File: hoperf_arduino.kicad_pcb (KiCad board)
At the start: 2 copper layers, 46 parts, among them J1 Conn_01x08_Male, J2 Conn_01x08_Male, Q1 DMN6140L, Q10 DMN6140L, Q11 DMN6140L, Q2 DMN6140L, Q3 DMN6140L, Q4 DMN6140L, Q5 DMN6140L, Q6 DMN6140L, Q7 DMN6140L, Q8 DMN6140L, Q9 DMN6140L, SW1 SW_SPST, U1 AZ1117-3.3, U2 RFM95W-915S2

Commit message: update sch and added routed pcb
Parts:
- removed J1, J2: Conn_01x08_Male, Connector_PinHeader_2.54mm:PinHeader_1x08_P2.54mm_Vertical
- added A1: Arduino_Nano_v3.x, Module:Arduino_Nano, F.Cu at (85.1, 120.7)
- added BT1: Battery_Cell, Connector_PinSocket_2.54mm:PinSocket_1x02_P2.54mm_Vertical, F.Cu at (156.2, 123.2)
- added FC1: FC-28, Connector_PinSocket_2.54mm:PinSocket_1x04_P2.54mm_Vertical, F.Cu at (62.2, 105.4)
- C1, C2, C3: footprint Capacitor_SMD:C_0603_1608Metric -> Capacitor_SMD:C_0603_1608Metric_Pad1.08x0.95mm_HandSolder
- D1: footprint LED_SMD:LED_0603_1608Metric -> LED_SMD:LED_0603_1608Metric_Pad1.05x0.95mm_HandSolder
- FB1, R1, R10, R11, R12, R13, R14, R15, R16, R17, R18, R19, R2, R20, R21, R22, R23, R24, R3, R4, R5, R6, R7, R8, R9: footprint Resistor_SMD:R_0603_1608Metric -> Resistor_SMD:R_0603_1608Metric_Pad0.98x0.95mm_HandSolder
- SW1: footprint Button_Switch_SMD:SW_SPST_SKQG_WithoutStem -> Button_Switch_SMD:SW_Push_1P1T_NO_CK_KSC7xxJ
- U1: footprint Package_TO_SOT_SMD:SOT-223-3_TabPin2 -> AZ1117CR-3.3:Diodes_Inc.-SOT89-03_2017-0-MFG
- moved R18 60.5 mm to (108.2, 111.4), turned to 270 degrees
- moved R19 58.4 mm to (110.2, 111.4), turned to 270 degrees
- moved R10 58.1 mm to (99.3, 95.2), turned to 270 degrees
- moved R11 56.6 mm to (101.3, 95.2), turned to 270 degrees
- moved Q9 56.6 mm to (109.2, 115.3), turned to 90 degrees
- moved Q5 53.4 mm to (100.3, 99.3), turned to 90 degrees
- moved R4 45.3 mm to (106.9, 80.9), turned to 270 degrees
- moved R5 44.9 mm to (109.0, 80.9), turned to 270 degrees
- moved R9 43.6 mm to (125.4, 80.9), turned to 270 degrees
- moved R8 42.5 mm to (123.2, 80.4), turned to 270 degrees
- moved R20 40.0 mm to (116.4, 111.4), turned to 270 degrees
- moved Q2 39.9 mm to (107.9, 85.1), turned to 90 degrees
- moved R12 39.1 mm to (107.2, 95.5), turned to 270 degrees
- moved R21 38.3 mm to (118.5, 111.4), turned to 270 degrees
- moved Q4 38.2 mm to (124.3, 85.1), turned to 90 degrees
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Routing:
- net +3V3: track 0.00 -> 281.7 mm, vias 0 -> 3
- net +5V: track 0.00 -> 217.8 mm, vias 0 -> 4
- net GND: track 0.00 -> 206.8 mm
- net /L_RESET: track 0.00 -> 110.0 mm, vias 0 -> 1
- net /L_SCK: track 0.00 -> 59.6 mm
- net /L_DIO3: track 0.00 -> 57.4 mm, vias 0 -> 1
- net /L_DIO0: track 0.00 -> 54.6 mm, vias 0 -> 1
- net /L_DIO4: track 0.00 -> 48.9 mm, vias 0 -> 1
- net /H_RESET: track 0.00 -> 47.8 mm
- net /L_DIO1: track 0.00 -> 47.4 mm, vias 0 -> 1
- net /H_DIO5: track 0.00 -> 47.4 mm, vias 0 -> 1
- net /H_DIO2: track 0.00 -> 45.9 mm
- net /H_CS: track 0.00 -> 44.5 mm
- net /H_DIO1: track 0.00 -> 40.9 mm
- net /L_DIO2: track 0.00 -> 40.4 mm, vias 0 -> 1
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
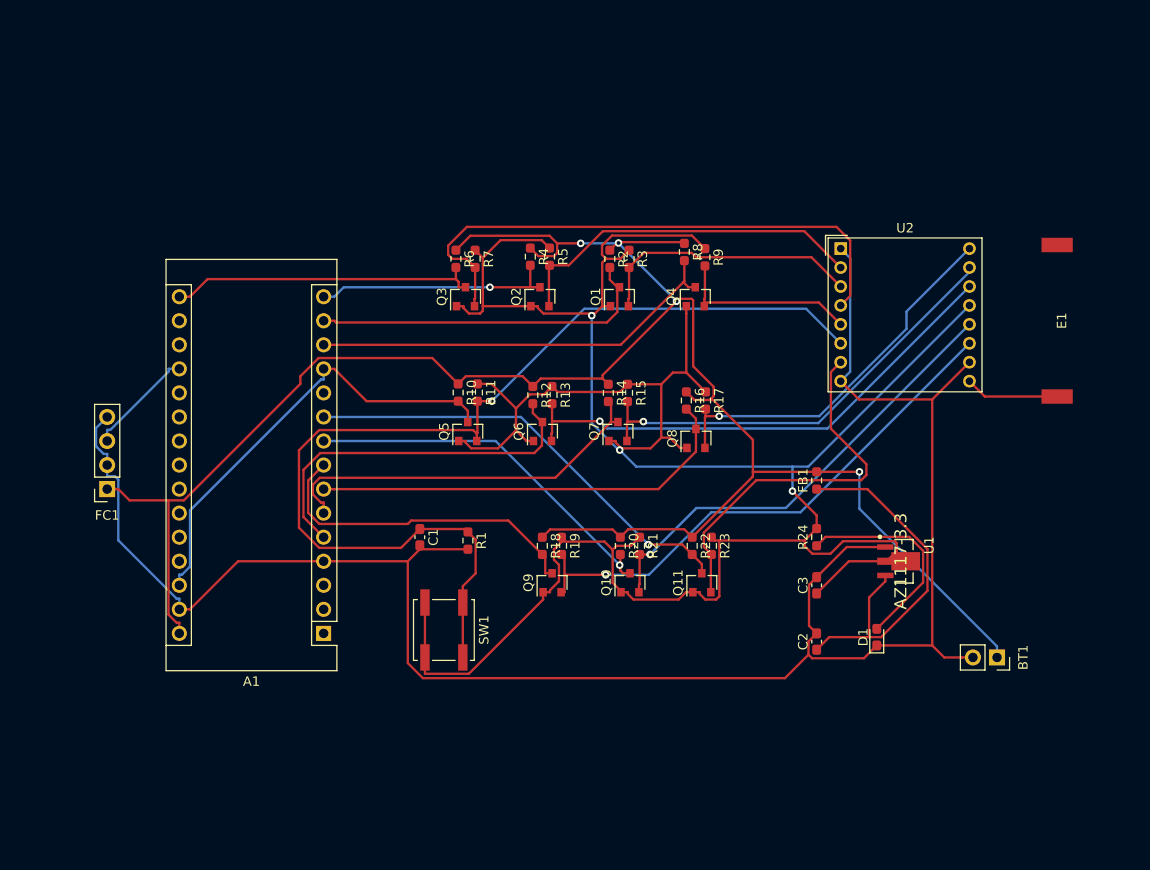
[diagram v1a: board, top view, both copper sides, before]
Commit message: remove unncessary parts, update sch
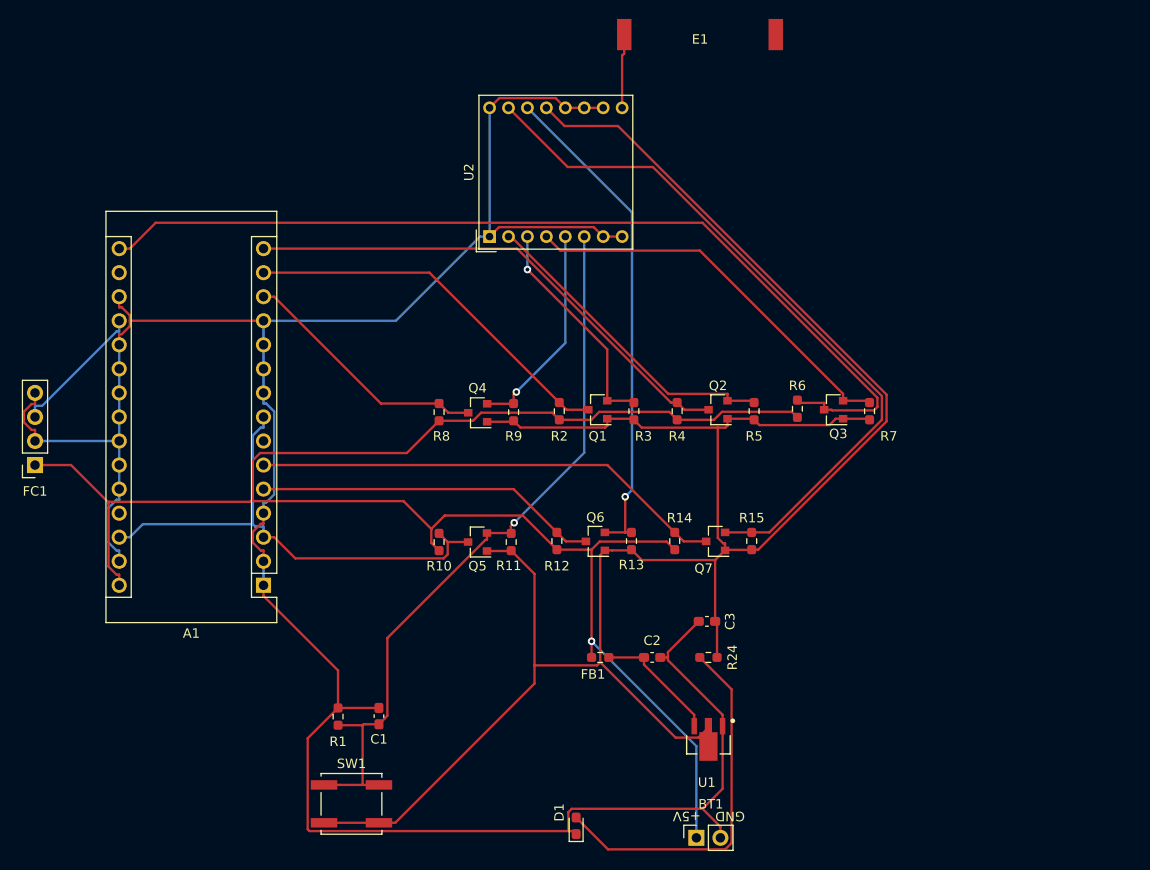
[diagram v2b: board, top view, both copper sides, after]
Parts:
- removed Q10, Q11, Q8, Q9: DMN6140L, Package_TO_SOT_SMD:SOT-23
- removed R16, R17, R18, R19, R20, R21, R22, R23: 10k, Resistor_SMD:R_0603_1608Metric_Pad0.98x0.95mm_HandSolder
- moved E1 48.3 mm to (124.8, 57.4), turned to 0 degrees
- moved R7 44.7 mm to (142.7, 97.2), turned to 90 degrees
- moved Q3 40.7 mm to (139.0, 97.0), turned to 180 degrees
- moved R6 39.4 mm to (135.1, 96.9), turned to 90 degrees
- moved D1 37.5 mm to (111.8, 141.0)
- moved U2 37.1 mm to (102.6, 78.7), turned to 90 degrees
- moved BT1 37.0 mm to (124.5, 142.2), turned to 90 degrees
- moved R8 30.9 mm to (97.3, 97.3), turned to 90 degrees
- moved FB1 29.5 mm to (114.3, 123.2), turned to 180 degrees
- moved U1 27.9 mm to (125.7, 132.1), turned to 180 degrees
- moved R5 27.1 mm to (130.6, 97.2), turned to 90 degrees
- moved Q4 26.0 mm to (101.4, 97.3), turned to 180 degrees
- moved R9 26.0 mm to (105.2, 97.3), turned to 90 degrees
- moved R1 23.1 mm to (86.6, 129.4), turned to 90 degrees
- moved R4 22.5 mm to (122.4, 97.2), turned to 90 degrees
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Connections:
- A1 pad 1: (no net) -> GND
- A1 pad 10: /H_DIO5 -> GND
- A1 pad 11: (no net) -> GND
- A1 pad 12: /H_RESET -> GND
- A1 pad 18: (no net) -> GND
- A1 pad 2: (no net) -> GND
- A1 pad 20: (no net) -> GND
- A1 pad 21: (no net) -> GND
- A1 pad 22: (no net) -> GND
- A1 pad 23: (no net) -> GND
- A1 pad 24: (no net) -> GND
- A1 pad 25: (no net) -> GND
- A1 pad 26: (no net) -> GND
- A1 pad 3: (no net) -> /H_RESET
- A1 pad 7: /H_DIO2 -> (no net)
- A1 pad 8: /H_DIO3 -> /H_RESET
- A1 pad 9: /H_DIO4 -> GND
- U2 pad 11: /L_DIO3 -> GND
- U2 pad 12: /L_DIO4 -> GND
- U2 pad 16: /L_DIO2 -> GND
- U2 pad 7: /L_DIO5 -> GND
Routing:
- net /H_SCK: track 32.9 -> 99.3 mm
- net GND: track 206.8 -> 267.9 mm
- net /L_DIO3: track 57.4 -> 0.00 mm, vias 1 -> 0
- net /L_DIO4: track 48.9 -> 0.00 mm, vias 1 -> 0
- net /H_DIO5: track 47.4 -> 0.00 mm, vias 1 -> 0
- net +3V3: track 281.7 -> 235.2 mm, vias 3 -> 0
- net /H_DIO2: track 45.9 -> 0.00 mm
- net /L_DIO2: track 40.4 -> 0.00 mm, vias 1 -> 0
- net /L_DIO5: track 40.2 -> 0.00 mm
- net /H_DIO4: track 39.6 -> 0.00 mm, vias 1 -> 0
- net /H_DIO3: track 35.4 -> 0.00 mm
- net /L_RESET: track 110.0 -> 78.6 mm
- net +5V: track 217.8 -> 187.5 mm, vias 4 -> 1
- net /L_DIO1: track 47.4 -> 76.0 mm, vias 1 -> 0
- net /H_MISO: track 25.6 -> 54.1 mm, vias 1 -> 0
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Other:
- board text added: "+5V"
- board text added: "GND"
